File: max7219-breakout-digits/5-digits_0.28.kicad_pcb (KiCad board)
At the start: 2 copper layers, 60 x 12 mm, 6 parts, among them J1 Conn_02x08_Odd_Even, U1 7Segment 3 digit CC_STH, U2 HDSM-443B_CC_2Digit_7Segment_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

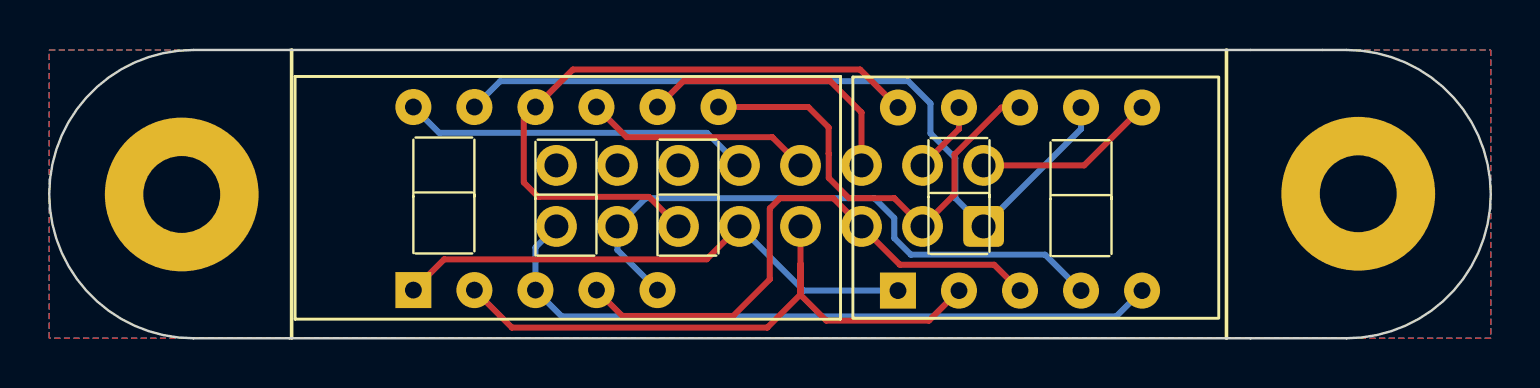
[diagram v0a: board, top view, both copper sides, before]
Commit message: rotate IDC on 0.28 displays, plated mounting holes for 0.35 displays, set version for 0.35 displays
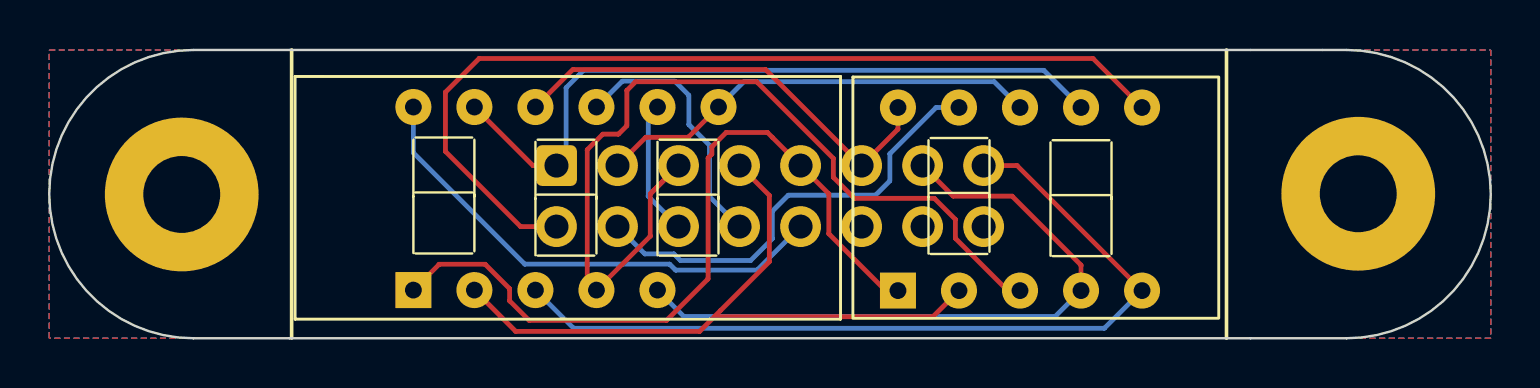
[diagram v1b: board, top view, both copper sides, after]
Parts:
- moved J1 18.0 mm to (87.2, 65.8), turned to -90 degrees
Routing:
- net /DIG0: track 7.59 -> 38.8 mm
- net /DIG1: track 3.04 -> 18.8 mm
- net /C: track 23.4 -> 38.8 mm
- net /E: track 22.4 -> 31.9 mm
- net /F: track 26.9 -> 18.9 mm
- net /DIG4: track 14.6 -> 20.8 mm
- net /DP: track 29.2 -> 35.3 mm
- net /DIG2: track 11.7 -> 5.66 mm
- net /D: track 26.5 -> 29.3 mm
- net /G: track 25.2 -> 27.9 mm
- net /A: track 32.5 -> 30.2 mm
- net /DIG3: track 9.50 -> 10.9 mm

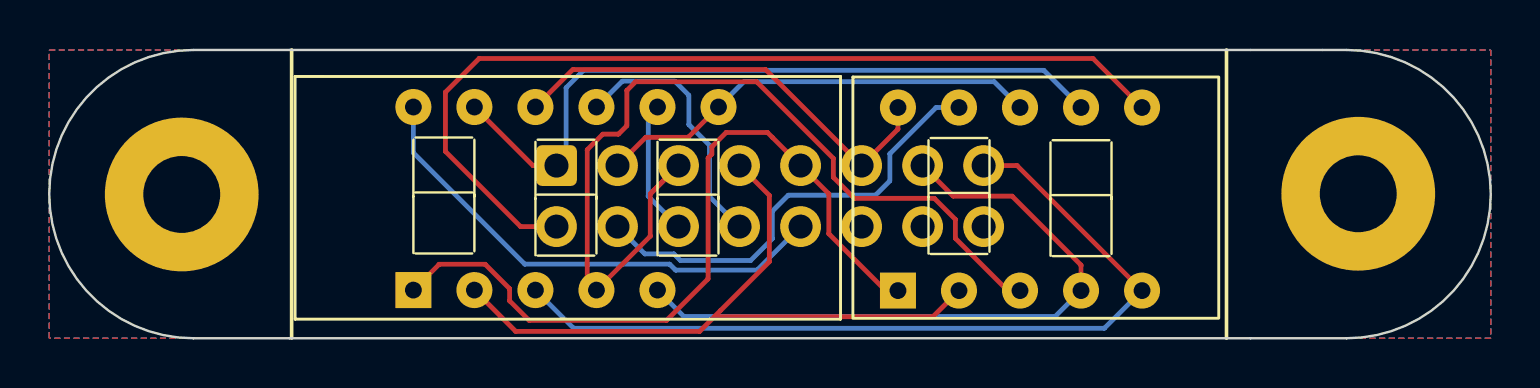
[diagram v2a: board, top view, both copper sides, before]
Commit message: add additional labels on front on backside from all boards
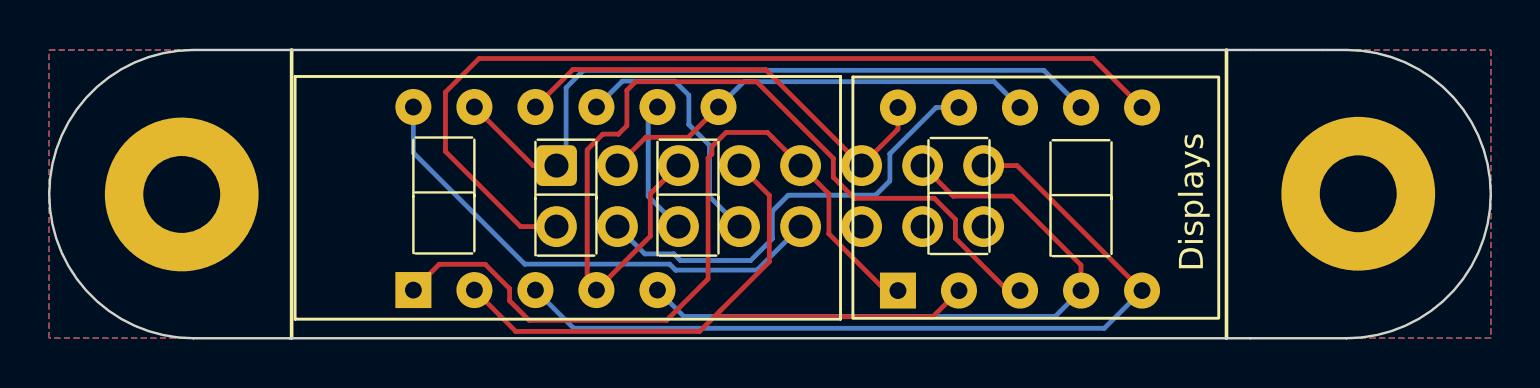
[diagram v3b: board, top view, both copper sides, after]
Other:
- board text added: "Displays"
- board text added: "IDC"
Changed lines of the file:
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@@
 		(layer "Edge.Cuts")
+	)
+	(gr_text "Displays"
+		(at 114.25 70.245639 90)
+		(layer "F.SilkS" knockout)
+		(effects
+			(font
+				(size 1 1)
+				(thickness 0.15)
+			)
+			(justify left bottom)
+		)
+	)
+	(gr_text "IDC"
+		(at 86.001394 64.363615 90)
+		(layer "B.SilkS" knockout)
+		(effects
+			(font
+				(size 2 2)
+				(thickness 0.25)
+			)
+			(justify left bottom mirror)
+		)
 	)
 	(gr_text "MobiFlight Display System 5 Digits ${REVISION}"
